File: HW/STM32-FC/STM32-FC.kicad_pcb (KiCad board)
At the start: 4 copper layers, 40 x 40 mm, 66 parts, among them J1 USB_B_Micro, J2 2.54mm Male, J3 Molex 53048-03, J4 PWM_Conn_3x04, J5 2.54mm Male, J6 2.54mm Male, Q1 S9013, Q2 S9013, U1 STM32F405RGTx, U2 USBLC6-2SC6, U3 AMS1117-3.3, U4 W25X40CLSN, U5 BMI088, U6 LIS2MDLTR, Y1 16MHz

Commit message: Big Update:IMU/RC/Conn./MCU
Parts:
- renumbered C1 to C2, C3 to C4, C5 to C7, J6 to J1

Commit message: Baro/SD Card update
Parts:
- removed the C2 at (132.9, 89.0)
- removed the C2 at (140.0, 85.5)
- removed the C4 at (132.9, 94.2)
- removed the C4 at (137.1, 89.1)
- removed the C7 at (149.4, 88.7)
- removed the C7 at (140.5, 101.4)
- removed the J1 at (166.5, 92.8)
- removed the J1 at (153.8, 82.7)
- removed JP1: Jumper, Jumper:SolderJumper-2_P1.3mm_Open_TrianglePad1.0x1.5mm
- added C1: 10pF, Capacitor_SMD:C_0402_1005Metric, F.Cu at (32.0, 58.6)
- added C2: 10uF, Capacitor_SMD:C_0402_1005Metric, F.Cu at (32.0, 60.5)
- added C23: 2.2nF, Capacitor_SMD:C_0402_1005Metric, F.Cu at (71.4, 107.1)
- added C24: 10nF, Capacitor_SMD:C_0402_1005Metric, F.Cu at (71.4, 109.1)
- added C25: 10uF, Capacitor_SMD:C_0402_1005Metric, F.Cu at (71.4, 111.0)
- added C26: 100nF, Capacitor_SMD:C_0402_1005Metric, F.Cu at (74.3, 107.1)
- added C27: 100nF, Capacitor_SMD:C_0402_1005Metric, F.Cu at (74.3, 109.1)
- added C28: 220nF, Capacitor_SMD:C_0402_1005Metric, F.Cu at (74.3, 111.0)
- added C29: 100nF, Capacitor_SMD:C_0402_1005Metric, F.Cu at (87.6, 132.3)
- added C29: 100nF, Capacitor_SMD:C_0402_1005Metric, F.Cu at (75.9, 113.3)
- added C3: 10pF, Capacitor_SMD:C_0402_1005Metric, F.Cu at (32.0, 62.5)
- added C30: 100nF, Capacitor_SMD:C_0402_1005Metric, F.Cu at (75.9, 115.8)
- added C31: 100nF, Capacitor_SMD:C_0402_1005Metric, F.Cu at (13.6, 113.9)
- added C32: 100nF, Capacitor_SMD:C_0402_1005Metric, F.Cu at (13.6, 115.8)
- added C33: 100nF, Capacitor_SMD:C_0402_1005Metric, F.Cu at (47.5, 120.0)
- added C34: 100nF, Capacitor_SMD:C_0402_1005Metric, F.Cu at (47.5, 122.0)
- added C4: 100nF, Capacitor_SMD:C_0402_1005Metric, F.Cu at (32.0, 64.5)
- added C5: 2.2uF, Capacitor_SMD:C_0402_1005Metric, F.Cu at (34.9, 58.6)
- added C7: 100nF, Capacitor_SMD:C_0402_1005Metric, F.Cu at (34.9, 62.5)
- added J1: PWM_Conn_3x08, PWM_Connector:PWM_Conn_3x08, F.Cu at (137.1, 111.5)
- added J10: GH 1.25mm 10P, JST_GH:JST_GH_BM10B-GHS-TBT_10, F.Cu at (129.5, 73.0)
- added J11: GH 1.25mm 6P, JST_GH:JST_GH_BM06B-GHS-TBT_06, F.Cu at (123.0, 98.5)
- added J12: GH 1.25mm 6P, JST_GH:JST_GH_BM06B-GHS-TBT_06, B.Cu at (151.0, 73.0)
- added J13: GH 1.25mm 6P, JST_GH:JST_GH_BM06B-GHS-TBT_06, B.Cu at (139.0, 73.0)
- added J14: GH 1.25mm 4P, JST_GH:JST_GH_BM04B-GHS-TBT_04, B.Cu at (123.0, 100.0)
- added J15: GH 1.25mm 4P, JST_GH:JST_GH_BM04B-GHS-TBT_04, F.Cu at (143.0, 73.0)
- added J16: GH 1.25mm 4P, JST_GH:JST_GH_BM04B-GHS-TBT_04, F.Cu at (153.0, 73.0)
- added J17: PWM_Conn_3x04, PWM_Connector:PWM_Conn_3x04, F.Cu at (152.3, 111.5)
- added J18: Micro_SD_Card_Det1, Connector_Card:microSD_HC_Hirose_DM3D-SF, B.Cu at (151.5, 87.0)
- added J6: PWM_Conn_3x01, PWM_Connector:PWM_Conn_3x01, F.Cu at (121.9, 111.5)
- added J7: ZH 1.5mm 3P, Connector_JST:JST_ZH_S3B-ZR-SM4A-TF_1x03-1MP_P1.50mm_Horizontal, F.Cu at (154.0, 83.8)
- added J8: ZH 1.5mm 4P, Connector_JST:JST_ZH_S4B-ZR-SM4A-TF_1x04-1MP_P1.50mm_Horizontal, F.Cu at (154.0, 92.8)
- added J9: PWM_Conn_3x01, PWM_Connector:PWM_Conn_3x01, F.Cu at (124.4, 111.5)
- added R14: 10k, Resistor_SMD:R_0402_1005Metric, F.Cu at (63.2, 88.3)
- added R15: 10k, Resistor_SMD:R_0402_1005Metric, F.Cu at (63.2, 90.3)
- added R16: 10k, Resistor_SMD:R_0402_1005Metric, F.Cu at (61.6, 114.8)
- added R17: 10k, Resistor_SMD:R_0402_1005Metric, F.Cu at (61.6, 116.8)
- added R18: 10k, Resistor_SMD:R_0402_1005Metric, F.Cu at (61.6, 118.8)
- added R19: 10k, Resistor_SMD:R_0402_1005Metric, F.Cu at (61.6, 120.8)
- added R20: 10k, Resistor_SMD:R_0402_1005Metric, F.Cu at (61.6, 122.8)
- added R21: 10k, Resistor_SMD:R_0402_1005Metric, F.Cu at (61.6, 124.8)
- added R22: 10k, Resistor_SMD:R_0402_1005Metric, F.Cu at (23.8, 113.9)
- added R23: 10k, Resistor_SMD:R_0402_1005Metric, F.Cu at (23.8, 115.9)
- added R24: 10k, Resistor_SMD:R_0402_1005Metric, F.Cu at (23.8, 117.9)
- added R25: 10k, Resistor_SMD:R_0402_1005Metric, F.Cu at (23.8, 119.9)
- added R26: 120, Resistor_SMD:R_0402_1005Metric, F.Cu at (23.8, 121.8)
- added R27: 120, Resistor_SMD:R_0402_1005Metric, F.Cu at (47.5, 124.0)
- added R29: 10k, Resistor_SMD:R_0402_1005Metric, F.Cu at (87.6, 122.4)
- added R31: 10k, Resistor_SMD:R_0402_1005Metric, F.Cu at (92.5, 126.0)
- added R32: 10k, Resistor_SMD:R_0402_1005Metric, F.Cu at (87.6, 124.3)
- added R33: 10k, Resistor_SMD:R_0402_1005Metric, F.Cu at (87.6, 126.3)
- added R34: 10k, Resistor_SMD:R_0402_1005Metric, F.Cu at (87.6, 128.3)
- added R35: 10k, Resistor_SMD:R_0402_1005Metric, F.Cu at (87.6, 130.3)
- added SW1: SK-02, SK-02:SK-02, B.Cu at (154.0, 99.5)
- added U10: ATA6561-GBQW, ATA6561:VDFN8_3X3_MCH_HandSolder, F.Cu at (142.0, 81.0)
- added U11: ATA6561-GBQW, ATA6561:VDFN8_3X3_MCH_HandSolder, F.Cu at (146.0, 81.0)
- added U12: LPS22HH, Package_LGA:ST_HLGA-10_2x2mm_P0.5mm_LayoutBorder3x2y, F.Cu at (92.9, 123.2)
- added U7: ICM-42688-P, ICM-42688-P:IIM42352_HandSolder, F.Cu at (137.0, 94.0)
- added U8: BMP280, Package_LGA:Bosch_LGA-8_2x2.5mm_P0.65mm_ClockwisePinNumbering, F.Cu at (141.0, 94.0)
- added U9: LIS2MDLTR, LIS2MDLTR:LIS2MDLTR_HandSolder, F.Cu at (137.0, 98.0)
- C14, C17, C18: value 100nF -> 10uF
- C15, C19: value 10uF -> 100nF
- C21: value 100nF -> 0.1nF
- C22: value 220nF -> 100nF
- D1, D2: value B5819W -> Red; footprint Diode_SMD:D_SOD-123 -> LED_SMD:LED_0603_1608Metric
- D3: value Red -> B5819W; footprint LED_SMD:LED_0603_1608Metric -> Diode_SMD:D_SOD-123
- D4: value Red -> Green
- D5: value Green -> Blue
- D6: value Blue -> B5819W; footprint LED_SMD:LED_0603_1608Metric -> Diode_SMD:D_SOD-123
- D7: value B5819W -> 1N4148
- H1, H2, H3, H4: footprint MountingHole:MountingHole_3.2mm_M3 -> MountingHole:MountingHole_2.7mm_M2.5
- J2: value 2.54mm Male -> GH 1.25mm 6P; footprint Connector_PinHeader_2.54mm:PinHeader_1x03_P2.54mm_Vertical -> JST_GH:JST_GH_BM06B-GHS-TBT_06; moved to B.Cu
- J3: value Molex 53048-03 -> USB_C_USB2.0_14P; footprint Connector_Molex:Molex_PicoBlade_53048-0310_1x03_P1.25mm_Horizontal -> Connector_USB:USB_C_Receptacle_GCT_USB4110
- J4: value PWM_Conn_3x04 -> GH 1.25mm 6P; footprint Custom_Parts:PWM_Conn_3x04 -> JST_GH:JST_GH_BM06B-GHS-TBT_06; moved to B.Cu
- J5: value 2.54mm Male -> JST ZH 1.5mm 2P; footprint Connector_PinHeader_2.54mm:PinHeader_1x02_P2.54mm_Vertical -> Connector_JST:JST_ZH_S2B-ZR-SM4A-TF_1x02-1MP_P1.50mm_Horizontal
- Q1, Q2: footprint digikey-footprints:SOT-23-3 -> Package_TO_SOT_SMD:SOT-23-3
- R10, R12: value 1k -> 10k
- R13: value 180 -> 1k
- R2: value 470 -> 4k7
- R3: value 1.5k -> 1k
- R4: value 10k -> 180
- R6: value 10k -> 1k
- R8: value 1k -> 5k1
- R9: value 1k -> 1k5
- TP1, TP2, TP3: value TestPoint -> Test Pin; footprint TestPoint:TestPoint_Pad_D1.0mm -> Connector_PinHeader_1.27mm:PinHeader_1x03_P1.27mm_Vertical
- U1: value STM32F405RGTx -> STM32F407VETx; footprint Package_QFP:LQFP-64_10x10mm_P0.5mm -> Package_QFP:LQFP-100_14x14mm_P0.5mm; moved to B.Cu
- U3: footprint Package_TO_SOT_SMD:SOT-223-3_TabPin2 -> Package_TO_SOT_SMD:SOT-89-3; moved to B.Cu
- U4: value W25X40CLSN -> AMS1117-3.3; footprint Package_SO:SOIC-8_3.9x4.9mm_P1.27mm -> Package_TO_SOT_SMD:SOT-89-3; moved to B.Cu
- U5: value BMI088 -> W25X40CLSN; footprint Custom_Parts:PQFN50P450X300X100-16N -> W25X40CLUX:USON_LUXIG_TR_HandSolder
- U6: value LIS2MDLTR -> BMI323; footprint Custom_Parts:PQFN50P200X200X70-12N -> BMI323:BMI323_HandSolder
- moved D2 135.2 mm to (32.7, 69.4), turned to 0 degrees
- moved D3 134.2 mm to (42.1, 59.3)
- moved D1 132.1 mm to (32.7, 66.8)
- moved R7 124.6 mm to (43.9, 89.0)
- moved C6 120.5 mm to (34.9, 60.5), turned to 0 degrees
- moved C8 119.5 mm to (34.9, 64.5)
- moved C9 116.6 mm to (37.8, 58.6), turned to 0 degrees
- moved R3 113.8 mm to (43.9, 81.1), turned to 0 degrees
- moved R5 113.1 mm to (43.9, 85.0), turned to 0 degrees
- moved R6 109.3 mm to (43.9, 87.0)
- moved BZ1 109.0 mm to (46.5, 95.0), turned to 0 degrees
- moved D7 109.0 mm to (50.3, 102.4), turned to 0 degrees
- moved R9 107.1 mm to (54.0, 77.2), turned to 0 degrees
- moved C10 105.5 mm to (37.8, 60.5)
- moved D4 103.9 mm to (32.7, 72.0)
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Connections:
- BZ1 pad 2: Net-(BZ1-Pad2) -> Net-(BZ1-+)
- C14 pad 1: +3.3V -> +5V
- C16 pad 1: +3.3V -> +3.3V_RC
- C18 pad 1: +3.3V -> +3.3V_RC
- C22 pad 1: /Sensors/MAG_C1 -> GND
- C22 pad 2: GND -> +3.3V
- C6 pad 1: GND -> /VCAP2
- C6 pad 2: /VCAP1 -> GND
- D1 pad 1: +5V -> Net-(D1-K)
- D1 pad 2: VBUS -> +3.3V
- D2 pad 1: +5V -> Net-(D2-K)
- D2 pad 2: Net-(D2-Pad2) -> /LED_RED
- D3 pad 1: Net-(D3-Pad1) -> +5V
- D3 pad 2: +3.3V -> Net-(BZ1-+)
- D4 pad 1: Net-(D4-Pad1) -> Net-(D4-K)
- D4 pad 2: /LED_RED -> /LED_GREEN
- D5 pad 1: Net-(D5-Pad1) -> Net-(D5-K)
- D5 pad 2: /LED_GREEN -> /LED_BLUE
- D6 pad 1: Net-(D6-Pad1) -> +5V
- D6 pad 2: /LED_BLUE -> VBUS
- D7 pad 1: +5V -> /UART1_TX
- D7 pad 2: Net-(BZ1-Pad2) -> /UART1_RX
- J2 pad 1: /UART1_RX_INV -> +3.3V
- J2 pad 2: +5V -> /SWDIO
- J2 pad 3: GND -> /SWCLK
- J4 pad 1: /TIM5_CH1 -> +5V
- J4 pad 2: /TIM5_CH2 -> +5V
- J4 pad 3: /TIM5_CH3 -> /PM_CURRENT
- J4 pad 4: /TIM5_CH4 -> /PM_VOLTAGE
- J4 pad 5: /PWM_5V -> GND
- J5 pad 1: /UART4_TX -> +BATT
- J5 pad 2: /UART4_RX -> GND
- Q1 pad 1: Net-(Q1-Pad1) -> Net-(Q1-B)
- Q1 pad 3: /UART1_RX -> Net-(BZ1-+)
- Q2 pad 3: Net-(BZ1-Pad2) -> /UART1_RX
- R10 pad 1: /V_BATT -> +BATT
- R10 pad 2: GND -> /V_BATT
- R11 pad 1: Net-(D5-Pad1) -> /V_BATT
- R12 pad 1: Net-(D6-Pad1) -> /TIM4_CH4
- R13 pad 1: /TIM3_CH4 -> /TIM4_CH4
- R3 pad 1: +3.3V -> Net-(D1-K)
- R3 pad 2: /USB_D+ -> GND
- R4 pad 1: +3.3V -> /TIM4_CH3
- R4 pad 2: /UART4_RX -> Net-(Q1-B)
- R5 pad 1: /UART1_RX_INV -> Net-(D2-K)
- R5 pad 2: Net-(Q1-Pad1) -> GND
- R6 pad 1: +3.3V -> Net-(D4-K)
- R6 pad 2: /UART1_RX -> GND
- R7 pad 1: Net-(D3-Pad1) -> Net-(D5-K)
- R8 pad 1: Net-(D4-Pad1) -> Net-(J3-CC1)
- R9 pad 1: +BATT -> +3.3V
- R9 pad 2: /V_BATT -> /USB_D+
- TP2 pad 1: /SPI1_MISO -> /SPI2_SCK
- TP3 pad 1: /SPI1_MOSI -> /SPI3_SCK
- U1 pad 1: +3.3V -> /LED_BLUE
- U1 pad 10: /LED_BLUE -> GND
- U1 pad 11: unconnected-(U1-Pad11) -> +3.3V
- U1 pad 12: GND -> /OSC_IN
- U1 pad 13: +3.3V -> /OSC_OUT
- U1 pad 14: /TIM5_CH1 -> /NRST
- U1 pad 15: /TIM5_CH2 -> /RSSI_IN
- U1 pad 16: /TIM5_CH3 -> /V_BATT
- U1 pad 17: /TIM5_CH4 -> /PM_CURRENT
- U1 pad 18: GND -> /PM_VOLTAGE
- U1 pad 2: unconnected-(U1-Pad2) -> /GYRO1_NSS
- U1 pad 20: unconnected-(U1-Pad20) -> GND
- U1 pad 21: /SPI1_SCK -> +3.3V
- U1 pad 22: /SPI1_MISO -> +3.3V
- U1 pad 23: /SPI1_MOSI -> /TIM5_CH1
- U1 pad 24: /V_BATT -> /TIM5_CH2
- U1 pad 25: unconnected-(U1-Pad25) -> /TIM5_CH3
- U1 pad 26: /GYRO_NSS -> /TIM5_CH4
- U1 pad 27: /ACC_NSS -> GND
- U1 pad 28: /MAG_NSS -> +3.3V
- U1 pad 3: unconnected-(U1-Pad3) -> /BARO_NSS
- U1 pad 30: unconnected-(U1-Pad30) -> /SPI1_SCK
- U1 pad 31: /VCAP1 -> /SPI1_MISO
- U1 pad 32: +3.3V -> /SPI1_MOSI
- U1 pad 33: /FLASH_NSS -> /CAN1_STBY
- U1 pad 34: /SPI2_SCK -> /CAN2_STBY
- U1 pad 35: /SPI2_MISO -> /TIM3_CH3
- U1 pad 36: /SPI2_MOSI -> /TIM3_CH4
- U1 pad 38: unconnected-(U1-Pad38) -> /BARO_INT
- U1 pad 39: unconnected-(U1-Pad39) -> /GPS1_LED
- U1 pad 4: unconnected-(U1-Pad4) -> /GYRO2_NSS
- U1 pad 40: /TIM3_CH4 -> /GPS1_BUZZER
- U1 pad 41: unconnected-(U1-Pad41) -> /GPS1_LED_SW
- U1 pad 42: unconnected-(U1-Pad42) -> /TIM1_CH2
- U1 pad 43: /UART1_RX -> unconnected-(U1-PE12-Pad43)
- U1 pad 44: /USB_D- -> /TIM1_CH3
- U1 pad 45: /USB_D+ -> /TIM1_CH4
- U1 pad 46: /SWDIO -> unconnected-(U1-PE15-Pad46)
- U1 pad 47: /VCAP2 -> /I2C2_SCL
- U1 pad 48: +3.3V -> /I2C2_SDA
- U1 pad 49: /SWCLK -> /VCAP1
- U1 pad 5: /OSC_IN -> /MAG_NSS
- U1 pad 50: unconnected-(U1-Pad50) -> +3.3V
- U1 pad 51: /UART4_TX -> /CAN2_RX
- U1 pad 52: /UART4_RX -> /SPI2_SCK
- U1 pad 53: unconnected-(U1-Pad53) -> /SPI2_MISO
- U1 pad 54: unconnected-(U1-Pad54) -> /SPI2_MOSI
- U1 pad 55: unconnected-(U1-Pad55) -> /UART3_TX
- U1 pad 56: unconnected-(U1-Pad56) -> /UART3_RX
- U1 pad 58: unconnected-(U1-Pad58) -> /UART3_CTS
- U1 pad 59: unconnected-(U1-Pad59) -> /UART3_RTS
- U1 pad 6: /OSC_OUT -> +3.3V
- U1 pad 60: /BOOT0 -> unconnected-(U1-PD13-Pad60)
- U1 pad 61: unconnected-(U1-Pad61) -> /TIM4_CH3
- U1 pad 62: unconnected-(U1-Pad62) -> /TIM4_CH4
- U1 pad 63: GND -> /TIM3_CH1
- U1 pad 64: +3.3V -> /TIM3_CH2
- U1 pad 7: /NRST -> /FLASH_NSS
- U1 pad 8: /LED_RED -> /MSD_NSS
- U1 pad 9: /LED_GREEN -> /MSD_DETECT
- U2 pad 1: /USB_CONN_D- -> /USB & POWER/USB_CONN_D-
- U2 pad 3: /USB_CONN_D+ -> /USB & POWER/USB_CONN_D+
- U4 pad 1: /FLASH_NSS -> GND
- U4 pad 2: /SPI2_MISO -> +3.3V_RC
- U4 pad 3: +3.3V -> +5V
- U5 pad 1: unconnected-(U5-Pad1) -> /FLASH_NSS
- U5 pad 2: GND -> /SPI2_MISO
- U5 pad 5: /GYRO_NSS -> /SPI2_MOSI
- U5 pad 6: GND -> /SPI2_SCK
- U5 pad 7: GND -> +3.3V
- U5 pad 8: /SPI1_SCK -> +3.3V
- U5 pad 9: /SPI1_MOSI -> unconnected-(U5-TP-Pad9)
- U6 pad 1: /SPI1_SCK -> /SPI3_MISO
- U6 pad 10: +3.3V -> unconnected-(U6-NC-Pad10)
- U6 pad 12: unconnected-(U6-Pad12) -> /GYRO2_NSS
- U6 pad 3: /MAG_NSS -> unconnected-(U6-NC-Pad3)
- U6 pad 4: /SPI1_MOSI -> unconnected-(U6-INT1-Pad4)
- U6 pad 5: /Sensors/MAG_C1 -> +3.3V
- U6 pad 7: /SPI1_MISO -> GND
- U6 pad 8: GND -> +3.3V
- U6 pad 9: +3.3V -> unconnected-(U6-INT2-Pad9)
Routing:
- net GND: track 47.5 -> 0.00 mm, vias 29 -> 0
- net +3.3V: track 46.7 -> 0.00 mm, vias 20 -> 0
- net +5V: track 36.8 -> 0.00 mm, vias 2 -> 0
- net /SPI1_MOSI: track 27.4 -> 0.00 mm, vias 2 -> 0
- net /NRST: track 26.4 -> 0.00 mm
- net /V_BATT: track 25.7 -> 0.00 mm, vias 2 -> 0
- net /SPI1_MISO: track 24.5 -> 0.00 mm, vias 2 -> 0
- net /SPI1_SCK: track 22.1 -> 0.00 mm, vias 2 -> 0
- net /TIM5_CH4: track 21.5 -> 0.00 mm, vias 2 -> 0
- net /TIM5_CH3: track 20.5 -> 0.00 mm
- net /TIM5_CH2: track 19.7 -> 0.00 mm
- net /TIM5_CH1: track 19.6 -> 0.00 mm
- net /TIM3_CH4: track 15.3 -> 0.00 mm, vias 2 -> 0
- net /SPI2_MISO: track 14.1 -> 0.00 mm
- net Net-(BZ1-Pad2): track 12.2 -> 0.00 mm
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- removed copper zone on F.Cu, net +3.3V
- removed copper zone on In2.Cu, net +3.3V
- removed copper zone on F.Cu, net +5V
- removed copper zone on F.Cu, net GND
- removed copper zone on In1.Cu, net GND
- removed copper zone on F.Cu, net VBUS
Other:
- board size 40 x 40 mm -> 38 x 47 mm
- copper layers 4 -> 2
- board text added: "CAN1"
- board text added: "CAN2"
- board text added: "DEBUG"
- board text added: "DSM"
- board text added: "GPS1"
- board text added: "GPS2"
- board text added: "I2C"
- board text added: "NARAE Flight Controller"
- board text added: "ON|OFF"
- board text added: "POWER"
- board text added: "RCIN|RSSI|MAIN CH 8-1|AUX CH 4-1|"
- board text added: "SRXL2"
- board text added: "TELEM1"
- board text added: "TELEM2"
- board text removed: "(5V)"
- board text removed: "1"
- board text removed: "2"
- board text removed: "3"
- board text removed: "3V3"
- board text removed: "4"
- board text removed: "5"
- board text removed: "5V"
- board text removed: "6"
- board text removed: "B"
- board text removed: "CLK"
- board text removed: "DIO"
- board text removed: "G"
- board text removed: "GND"
- board text removed: "IMU"
- board text removed: "JLCJLCJLCJLC"
- board text removed: "MISO"
- board text removed: "MOSI"
- board text removed: "Mag"
- board text removed: "NRST"
- board text removed: "PWM"
- board text removed: "PWR"
- board text removed: "R"
- board text removed: "Rx4"
- board text removed: "SBUS"
- board text removed: "SCK"
- board text removed: "SWD"
- board text removed: "Tx4"
- board text removed: "X"
- board text removed: "Y"
- board text removed: "Z"
- board text removed: "casterian.net STM32 Flight Controller Rev. B 2022.12.10."
- board text removed: "~{Rx}1"

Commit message: 2025.01.16
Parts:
- removed the C29 at (75.9, 113.3)
- removed the C30 at (75.9, 115.8)
- removed the J6 at (121.9, 111.5)
- removed the U3 at (135.0, 104.0)
- removed the U7 at (137.0, 94.0)
- removed the U8 at (141.0, 94.0)
- added C28: 4.7u, Capacitor_SMD:C_0402_1005Metric, F.Cu at (141.0, 92.0)
- added J8: PWM_Conn_3x01, PWM_Connector:PWM_Conn_3x01, F.Cu at (124.4, 111.5)
- added U2: AMS1117-3.3, Package_TO_SOT_SMD:SOT-89-3, B.Cu at (136.0, 103.0)
- added U6: ICM-42688-P, ICM-42688-P:IIM42352_HandSolder, F.Cu at (137.0, 94.0)
- C10: renamed from C3; moved to B.Cu
- C11: renamed from C5; moved to B.Cu
- C12: renamed from C6; moved to B.Cu
- C13, C18, R1, R2, Y1: moved to B.Cu
- C14: renamed from C15; moved to B.Cu
- C15: renamed from C17; moved to B.Cu
- C16: renamed from C14; moved to B.Cu
- C17: renamed from C16; moved to B.Cu
- C19: renamed from C29; moved to B.Cu
- C9: renamed from C1; moved to B.Cu
- D5: renamed from D3; footprint Diode_SMD:D_SOD-123 -> Diode_SMD:D_SOD-323
- D6: footprint Diode_SMD:D_SOD-123 -> Diode_SMD:D_SOD-323
- D7: footprint Diode_SMD:D_SOD-123 -> Diode_SMD:D_SOD-523
- H1, H2, H3, H4: footprint MountingHole:MountingHole_2.7mm_M2.5 -> MountingHole:MountingHole_2.2mm_M2
- J6: renamed from J18; footprint Connector_Card:microSD_HC_Hirose_DM3D-SF -> Connector_Card:microSD_HC_Molex_104031-0811
- R10: renamed from R32; moved to B.Cu
- R11: renamed from R33; moved to B.Cu
- R12: renamed from R34; moved to B.Cu
- R13: renamed from R35; moved to B.Cu
- R14: renamed from R29; moved to B.Cu
- R28: renamed from R22; moved to B.Cu
- R30: renamed from R23; moved to B.Cu
- R32: renamed from R24; moved to B.Cu
- R33: renamed from R25; moved to B.Cu
- U7: renamed from U9; footprint LIS2MDLTR:LIS2MDLTR_HandSolder -> LIS2MDLTR:LIS2MDLTR
- moved C31 139.6 mm to (149.0, 80.0), turned to 90 degrees
- moved C32 139.6 mm to (149.0, 82.0), turned to -90 degrees
- moved R28 129.0 mm to (147.2, 76.5)
- moved R30 127.6 mm to (145.2, 76.5), turned to 180 degrees
- moved R29 125.5 mm to (141.5, 78.2)
- moved C9 119.5 mm to (143.2, 102.2)
- moved C10 116.2 mm to (141.2, 102.2)
- moved C1 112.0 mm to (135.5, 103.5), turned to 90 degrees
- moved C2 111.5 mm to (136.5, 103.5), turned to 90 degrees
- moved C6 111.3 mm to (140.5, 103.5), turned to 90 degrees
- moved C5 111.2 mm to (139.5, 103.5), turned to 90 degrees
- moved C4 110.7 mm to (138.5, 103.5), turned to 90 degrees
- moved C3 110.5 mm to (137.5, 103.5), turned to 90 degrees
- moved R31 109.1 mm to (146.5, 78.2)
- moved C12 108.0 mm to (141.0, 81.0), turned to 90 degrees
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- renumbered C2 to C1, C4 to C2, C19 to C20, C25 to C21, C26 to C22, C27 to C23, C21 to C24, C23 to C25, C24 to C26, C28 to C27, C20 to C29, C7 to C3, C22 to C30, C8 to C4, C9 to C5, C10 to C6, C11 to C7, C12 to C8, D4 to D3, D5 to D4, J2 to J1, J7 to J10, J8 to J11, J10 to J12, J11 to J13, J15 to J14, J12 to J15, J13 to J17, J14 to J18, J1 to J2, J17 to J3, J3 to J4, J4 to J5, J5 to J7, R10 to R15, R11 to R16, R31 to R17, R14 to R18, R13 to R19, R12 to R20, R15 to R21, R16 to R22, R17 to R23, R19 to R24, R18 to R25, R20 to R26, R21 to R27, R26 to R29, R27 to R31, R5 to R4, R6 to R5, R7 to R6, R4 to R7, TP2 to TP1, TP1 to TP2, U2 to U3, U6 to U8, U12 to U9
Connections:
- J9 pad 1: /RSSI_IN -> /TIM4_CH4
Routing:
- added copper zone on In2.Cu, net +3.3V
- added copper zone on In1.Cu, net +5V
- added copper zone on B.Cu, net GND
- added copper zone on F.Cu, net GND
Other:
- board size 38 x 47 mm -> 38 x 48 mm
- copper layers 2 -> 4

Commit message: 2025.01.17 : PCB layout
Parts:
- removed the J2 at (137.1, 111.5)
- removed the J3 at (152.3, 111.5)
- removed the J8 at (124.4, 111.5)
- removed the J9 at (121.9, 111.5)
- removed SW1: SK-02, SK-02:SK-02
- added J6: PWM_Conn_3x14, PWM_Connector:PWM_Conn_3x14, B.Cu at (139.0, 111.5)
- added R2: 100k, Resistor_SMD:R_0402_1005Metric, B.Cu at (154.5, 103.0)
- added SW2: SW_DIP_x03, Button_Switch_SMD:SW_DIP_SPSTx03_Slide_KingTek_DSHP03TJ_W5.25mm_P1.27mm_JPin, B.Cu at (154.0, 98.2)
- H1, H2, H3, H4: footprint MountingHole:MountingHole_2.2mm_M2 -> Hole:MountingHole_2.2mm_M2
- J5: renamed from J7; footprint Connector_JST:JST_ZH_S2B-ZR-SM4A-TF_1x02-1MP_P1.50mm_Horizontal -> JST_ZH:JST_ZH_S2B-ZR-SM4A-TF_1x02-1MP_P1.50mm_Horizontal
- J7: renamed from J10; footprint Connector_JST:JST_ZH_S3B-ZR-SM4A-TF_1x03-1MP_P1.50mm_Horizontal -> JST_ZH:JST_ZH_S3B-ZR-SM4A-TF_1x03-1MP_P1.50mm_Horizontal
- J8: renamed from J11; footprint Connector_JST:JST_ZH_S4B-ZR-SM4A-TF_1x04-1MP_P1.50mm_Horizontal -> JST_ZH:JST_ZH_S4B-ZR-SM4A-TF_1x04-1MP_P1.50mm_Horizontal
- U10, U11: footprint ATA6561:VDFN8_3X3_MCH_HandSolder -> ATA6561:VDFN8_3X3_MCH-L
- U5: footprint W25X40CLUX:USON_LUXIG_TR_HandSolder -> W25X40CLUX:USON_LUXIG TR_WIN-L
- U6: renamed from U8; footprint BMI323:BMI323_HandSolder -> BMI323:BMI323_L
- U7: renamed from U6; footprint ICM-42688-P:IIM42352_HandSolder -> ICM-42688-P:IIM42352_L
- U8: renamed from U7; value LIS2MDLTR -> LGA-12
- U9: footprint Package_LGA:ST_HLGA-10_2x2mm_P0.5mm_LayoutBorder3x2y -> LPS22HH:ST_HLGA-10_2x2mm_P0.5mm_LayoutBorder3x2y
- moved R1 10.7 mm to (152.2, 103.0)
- moved R9 2.85 mm to (126.5, 93.8)
- moved C24 2.00 mm to (136.5, 90.2), turned to 180 degrees
- moved TP2 1.00 mm to (149.0, 101.5)
- moved C5 0.50 mm to (128.0, 83.0)
- moved H1 0.50 mm to (123.0, 77.5)
- moved H2 0.50 mm to (155.0, 77.5)
- moved U2 0.50 mm to (131.0, 87.5)
- moved C11 0.25 mm to (132.5, 100.2)
- moved C12 0.25 mm to (131.5, 100.2)
- moved J2 0.25 mm to (123.8, 85.8)
- moved R31 0.25 mm to (127.0, 100.2)
- moved U1 0.25 mm to (135.8, 91.0)
- moved C28 0.09 mm to (136.5, 101.5)
- renumbered C9 to C1, C6 to C10, C7 to C11, C8 to C12, C16 to C14, C14 to C15, C17 to C16, C15 to C17, C20 to C19, C1 to C2, C19 to C20, C29 to C21, C24 to C22, C30 to C23, C25 to C24, C26 to C25, C28 to C26, C21 to C27, C22 to C28, C23 to C29, C2 to C3, C27 to C30, C33 to C32, C32 to C33, C10 to C4, C11 to C5, C12 to C6, C3 to C7, C4 to C8, C5 to C9, D5 to D3, D3 to D4, D4 to D5, J13 to J10, J15 to J11, J17 to J12, J18 to J13, J16 to J15, J4 to J2, J5 to J3, J6 to J4, J12 to J9, R9 to R10, R10 to R11, R11 to R12, R12 to R13, R13 to R14, R14 to R15, R17 to R16, R15 to R17, R16 to R18, R21 to R19, R19 to R21, R18 to R22, R22 to R23, R23 to R24, R24 to R26, R26 to R27, R27 to R28, R28 to R29, R2 to R3, R32 to R31, R33 to R32, R29 to R33, R31 to R34, R3 to R4, R7 to R5, R4 to R6, R5 to R7, R6 to R8, R8 to R9, U3 to U2, U2 to U3
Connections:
- J8 pad 1: /UART1_RX -> /UART1_TX
- R1 pad 1: /BOOT0 -> GND
- R1 pad 2: GND -> /BOOT0
- U1 pad 77: unconnected-(U1-PA15-Pad77) -> /BOOT1
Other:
- board text added: "NARAE STM32 FC"
- board text added: "RCIN|RSSI|AUX CH 4-1|MAIN CH 8-1|"
- board text added: "SPI1"
- board text added: "SPI2"
- board text added: "SPI3"
- board text removed: "NARAE Flight Controller"
- board text removed: "RCIN|RSSI|MAIN CH 8-1|AUX CH 4-1|"

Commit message: 2025.01.17 Differential Pair update
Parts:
- removed D7: 1N4148, Diode_SMD:D_SOD-523
- U8: value LGA-12 -> LIS2MDLTR
- moved U2 0.50 mm to (131.5, 87.5)
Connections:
- net /Communication/CAN1_H renamed /Communication/CAN1_P
- net /Communication/CAN1_L renamed /Communication/CAN1_N
- net /Communication/CAN2_H renamed /Communication/CAN2_P
- net /Communication/CAN2_L renamed /Communication/CAN2_N

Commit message: 2025.02.01 PCB Routing start
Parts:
- added R35: 0, Resistor_SMD:R_0402_1005Metric, F.Cu at (122.5, 116.0)
- C1, C20, C4, R11, R12, R13, R14, R15, R3, Y1: moved to F.Cu
- C11, C12, D3, R4, R5, R6, R7, R8: moved to B.Cu
- D1: value Red -> White; footprint LED_SMD:LED_0603_1608Metric -> LED_SMD:LED_0402_1005Metric; moved to B.Cu
- D2, D4, D5: footprint LED_SMD:LED_0603_1608Metric -> LED_SMD:LED_0402_1005Metric; moved to B.Cu
- J4: footprint Connector_Card:microSD_HC_Molex_104031-0811 -> Connector_Card:microSD_HC_Hirose_DM3D-SF
- moved C12 22.4 mm to (142.0, 80.5), turned to 180 degrees
- moved R4 21.6 mm to (148.2, 103.8), turned to 0 degrees
- moved C11 21.0 mm to (142.0, 81.5), turned to 180 degrees
- moved R6 19.8 mm to (148.2, 100.8), turned to 0 degrees
- moved R7 19.6 mm to (148.2, 101.8), turned to 0 degrees
- moved R8 19.5 mm to (148.2, 102.8), turned to 0 degrees
- moved D1 17.9 mm to (146.2, 103.8), turned to 180 degrees
- moved D2 15.6 mm to (146.2, 100.8), turned to 180 degrees
- moved D4 15.4 mm to (146.2, 101.8), turned to 180 degrees
- moved D5 15.2 mm to (146.2, 102.8), turned to 180 degrees
- moved C29 11.6 mm to (140.8, 90.4), turned to 0 degrees
- moved C8 11.5 mm to (131.6, 94.2), turned to 0 degrees
- moved C10 11.5 mm to (131.6, 96.2), turned to 0 degrees
- moved C9 11.4 mm to (131.6, 95.2), turned to 0 degrees
- moved C28 11.0 mm to (140.8, 91.4), turned to 0 degrees
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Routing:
- net /UART1_TX: track 0.00 -> 58.8 mm
- net /UART2_RX: track 0.00 -> 30.1 mm, vias 0 -> 2
- net /UART2_TX: track 0.00 -> 25.6 mm, vias 0 -> 2
- net /TIM4_CH4: track 0.00 -> 17.8 mm
- net /USB_D+: track 0.00 -> 11.1 mm, vias 0 -> 1
- net /USB_D-: track 0.00 -> 10.3 mm, vias 0 -> 1
- net +3.3V: track 0.00 -> 10.2 mm
- net /Communication/CAN2_N: track 0.00 -> 10.0 mm
- net GND: track 0.00 -> 9.83 mm
- net /Communication/CAN2_P: track 0.00 -> 9.62 mm
- net /UART2_RTS: track 0.00 -> 7.28 mm
- net /Communication/CAN1_P: track 0.00 -> 6.02 mm
- net /Communication/CAN1_N: track 0.00 -> 6.02 mm
- net /USB & POWER/USB_CONN_D+: track 0.00 -> 3.97 mm
- net /USB & POWER/USB_CONN_D-: track 0.00 -> 3.16 mm
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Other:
- board text removed: "ON|OFF"

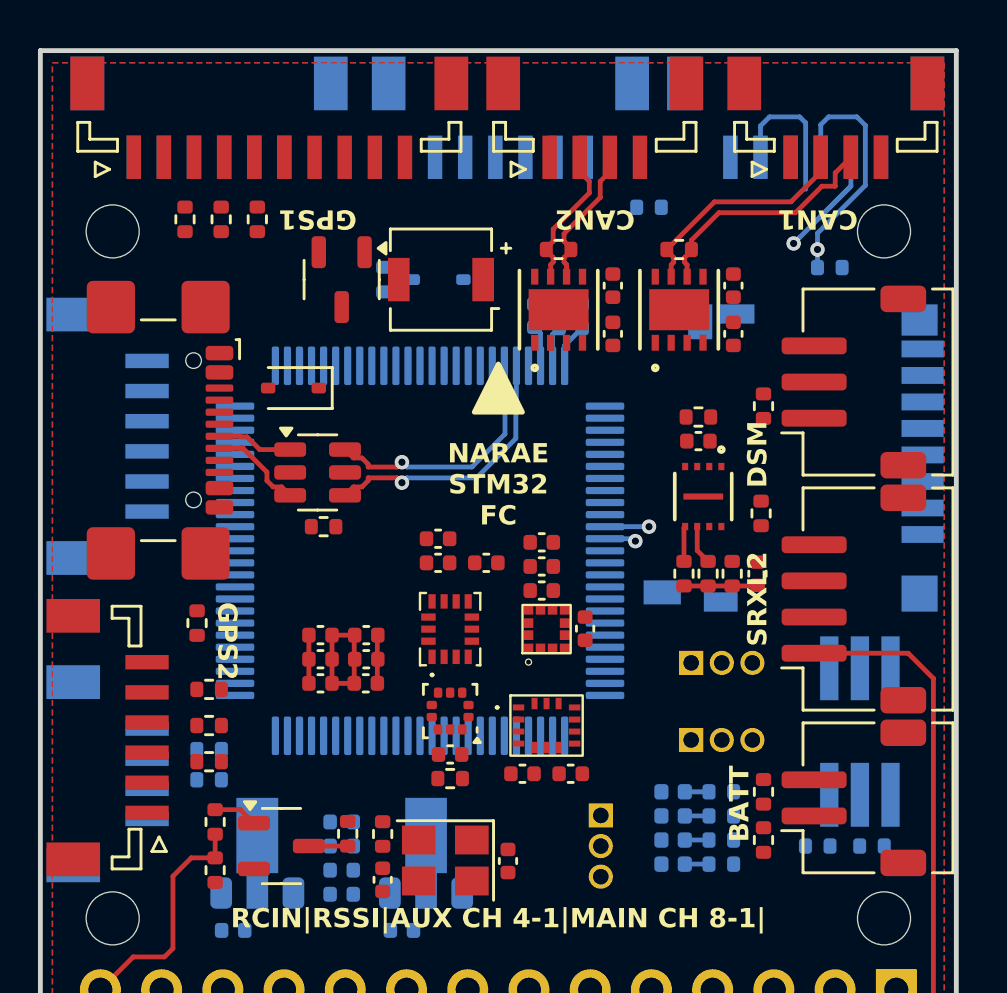
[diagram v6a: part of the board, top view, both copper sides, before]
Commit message: 2025.02.01 PCB routing update 1
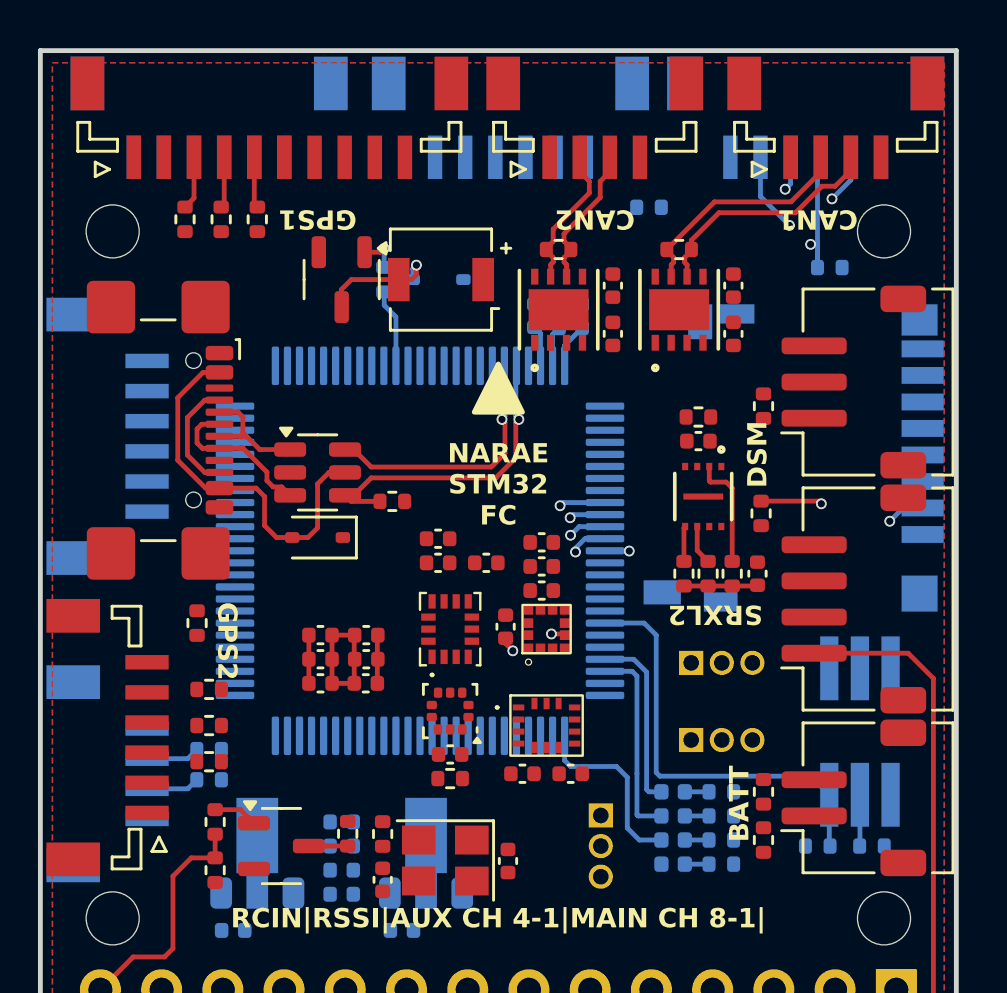
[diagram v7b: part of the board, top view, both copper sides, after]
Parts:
- moved D6 6.28 mm to (131.5, 90.2)
- moved C30 3.30 mm to (139.3, 93.9)
- moved R10 3.04 mm to (134.6, 88.7), turned to 180 degrees
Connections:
- J13 pad 2: /I2C3_SCL -> /I2C1_SCL
- J13 pad 3: /I2C3_SDA -> /I2C1_SDA
- J9 pad 4: /I2C1_SCL -> /I2C3_SCL
- J9 pad 5: /I2C1_SDA -> /I2C3_SDA
- R23 pad 2: /I2C1_SDA -> /I2C3_SDA
- R24 pad 2: /I2C1_SCL -> /I2C3_SCL
- R31 pad 2: /I2C3_SDA -> /I2C1_SDA
- R32 pad 2: /I2C3_SCL -> /I2C1_SCL
- U1 pad 2: /GYRO1_NSS -> /GYRO2_NSS
- U1 pad 3: /BARO_NSS -> /MAG_NSS
- U1 pad 4: /GYRO2_NSS -> /GYRO1_NSS
- U1 pad 5: /MAG_NSS -> /BARO_NSS
- U1 pad 8: /MSD_NSS -> unconnected-(U1-PC14-Pad8)
- U1 pad 88: unconnected-(U1-PD7-Pad88) -> /MSD_NSS
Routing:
- net /UART2_CTS: track 0.00 -> 25.3 mm, vias 0 -> 2
- net /UART2_RTS: track 7.28 -> 25.6 mm, vias 0 -> 2
- net /BOOT0: track 0.00 -> 17.7 mm
- net /MSD_NSS: track 0.00 -> 17.4 mm, vias 0 -> 3
- net VBUS: track 0.00 -> 15.9 mm
- net /LED_GREEN: track 0.00 -> 8.19 mm
- net /LED_BLUE: track 0.00 -> 7.64 mm
- net /LED_RED: track 0.00 -> 7.47 mm
- net Net-(BZ1-+): track 0.00 -> 5.15 mm, vias 0 -> 1
- net Net-(J2-CC1): track 0.00 -> 4.81 mm
- net /SPI2_MISO: track 0.00 -> 4.71 mm
- net /TIM4_CH3: track 0.00 -> 3.27 mm
- net /Sensors/MAG_C1: track 0.00 -> 3.10 mm, vias 0 -> 2
- net /USB & POWER/USB_CONN_D+: track 3.97 -> 6.58 mm
- net /UART4_RX: track 0.00 -> 2.22 mm
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
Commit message: 2025.02.03 PCB routing update 2
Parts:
- moved R1 8.50 mm to (152.3, 94.5)
- moved R2 8.50 mm to (154.6, 94.5)
- moved R16 4.43 mm to (135.0, 96.2), turned to -90 degrees
- moved TP2 2.54 mm to (143.2, 104.3), turned to 0 degrees
- moved R30 1.58 mm to (143.8, 77.0), turned to 90 degrees
- moved SW2 0.95 mm to (154.0, 99.2), turned to 90 degrees
- moved R12 0.30 mm to (147.4, 91.7)
- moved R13 0.30 mm to (146.4, 91.7)
- moved C20 0.25 mm to (150.0, 91.7)
- moved C14 0.10 mm to (135.0, 106.4)
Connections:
- J6 pad 1: /TIM5_CH1 -> /TIM4_CH2
- J6 pad 10: /TIM1_CH2 -> /TIM3_CH4
- J6 pad 11: /TIM1_CH3 -> /TIM1_CH2
- J6 pad 12: /TIM1_CH4 -> /TIM1_CH3
- J6 pad 14: /TIM4_CH4 -> /TIM1_CH4
- J6 pad 2: /TIM5_CH2 -> /TIM4_CH4
- J6 pad 3: /TIM5_CH3 -> /TIM3_CH1
- J6 pad 4: /TIM5_CH4 -> /TIM3_CH2
- J6 pad 5: /TIM3_CH1 -> /TIM5_CH1
- J6 pad 6: /TIM3_CH2 -> /TIM5_CH2
- J6 pad 7: /TIM3_CH3 -> /TIM5_CH3
- J6 pad 8: /TIM3_CH4 -> /TIM5_CH4
- J6 pad 9: /TIM4_CH2 -> /TIM3_CH3
- R20 pad 1: /TIM4_CH4 -> /TIM1_CH4
- R21 pad 1: /TIM4_CH4 -> /TIM1_CH4
- R35 pad 2: /TIM4_CH4 -> /TIM1_CH4
- SW2 pad 1: +3.3V -> +5V_PWM
- SW2 pad 3: +5V_PWM -> +3.3V
- SW2 pad 4: +5V -> /BOOT0
- SW2 pad 6: /BOOT0 -> +5V
- TP1 pad 2: /SPI2_MOSI -> /SPI2_MISO
- TP1 pad 3: /SPI2_MISO -> /SPI2_MOSI
- TP2 pad 2: /SPI1_MOSI -> /SPI1_MISO
- TP2 pad 3: /SPI1_MISO -> /SPI1_MOSI
- TP3 pad 2: /SPI3_MOSI -> /SPI3_MISO
- TP3 pad 3: /SPI3_MISO -> /SPI3_MOSI
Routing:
- net GND: track 9.83 -> 150.4 mm, vias 0 -> 16
- net /UART1_RX: track 1.62 -> 118.3 mm, vias 0 -> 3
- net +3.3V: track 10.2 -> 93.6 mm, vias 0 -> 20
- net +5V: track 0.00 -> 55.5 mm, vias 0 -> 14
- net +5V_PWM: track 0.00 -> 40.1 mm, vias 0 -> 1
- net /PM_VOLTAGE: track 0.00 -> 31.8 mm, vias 0 -> 2
- net /PM_CURRENT: track 0.00 -> 31.0 mm, vias 0 -> 2
- net /SPI2_MOSI: track 1.47 -> 31.4 mm, vias 0 -> 2
- net /SPI2_SCK: track 1.63 -> 30.1 mm, vias 0 -> 2
- net /SPI2_MISO: track 4.71 -> 33.2 mm, vias 0 -> 2
- net /UART4_TX: track 0.00 -> 27.3 mm, vias 0 -> 2
- net /I2C3_SCL: track 2.12 -> 27.9 mm, vias 0 -> 1
- net /SPI1_SCK: track 0.00 -> 25.7 mm, vias 0 -> 2
- net /SWCLK: track 0.00 -> 25.5 mm, vias 0 -> 2
- net /UART4_RX: track 2.22 -> 27.6 mm, vias 0 -> 2
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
